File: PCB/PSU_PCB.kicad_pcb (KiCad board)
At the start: 2 copper layers, 169.3 x 128 mm, 130 parts, among them CON1 BARREL_JACK, IC1 ATMEGA328-P, P1 USB_OTG, P2 FTDI, P3 V+, P4 V-, P5 ISP, P6 I2C, P7 LCD_Display, Q1 TIP32CG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

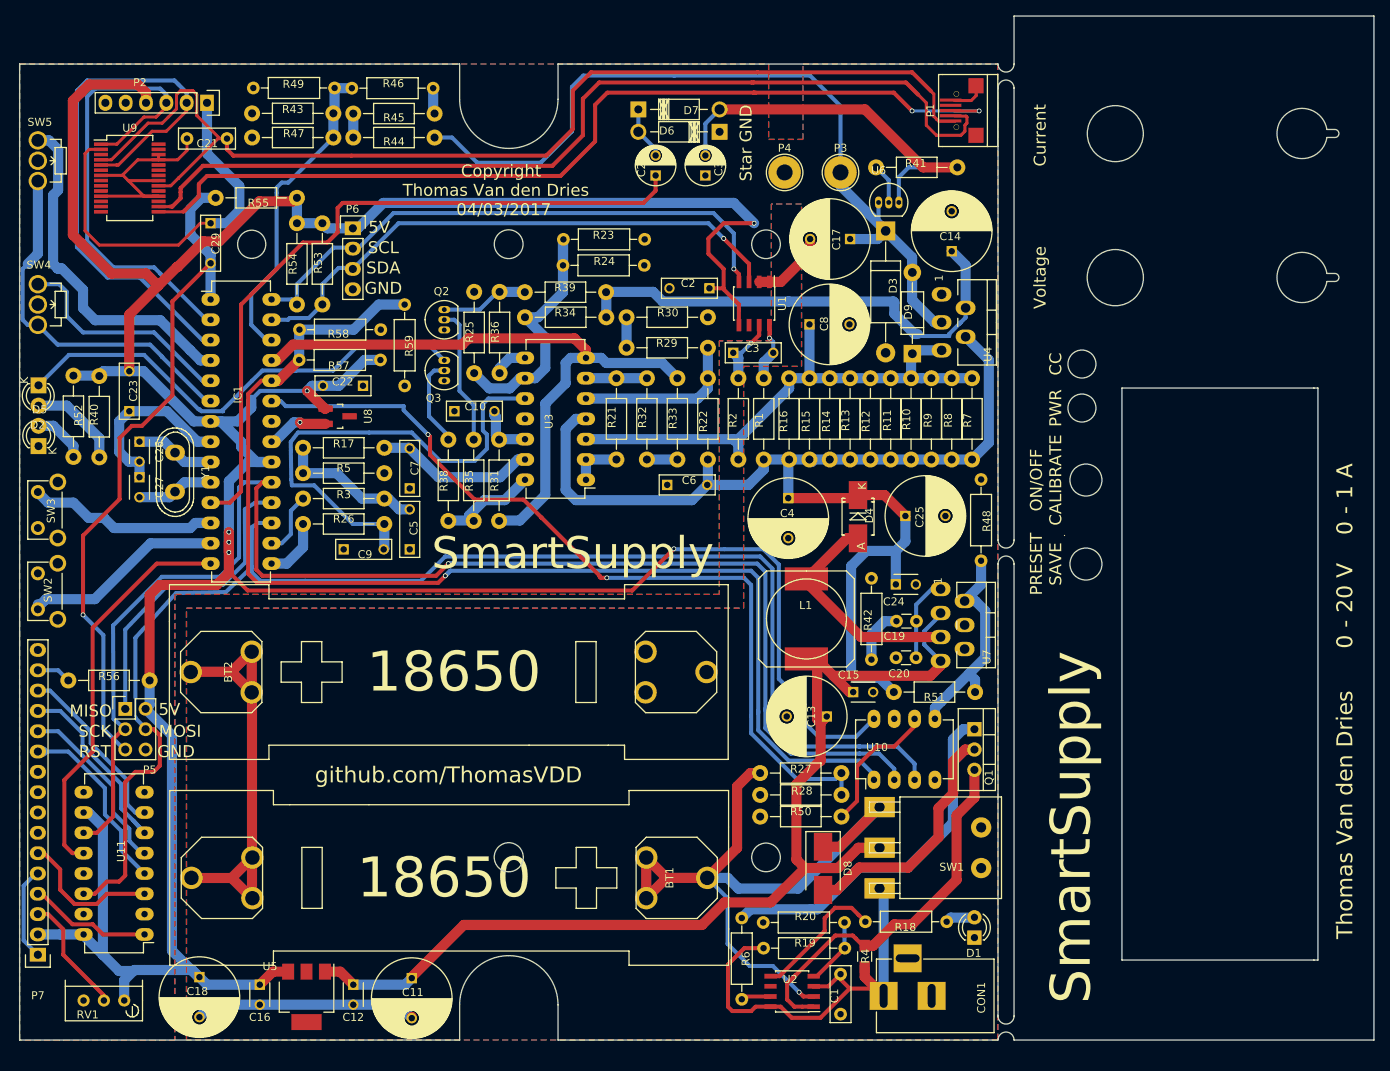
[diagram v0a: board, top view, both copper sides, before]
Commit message: Added protection resistor to charging circuitry
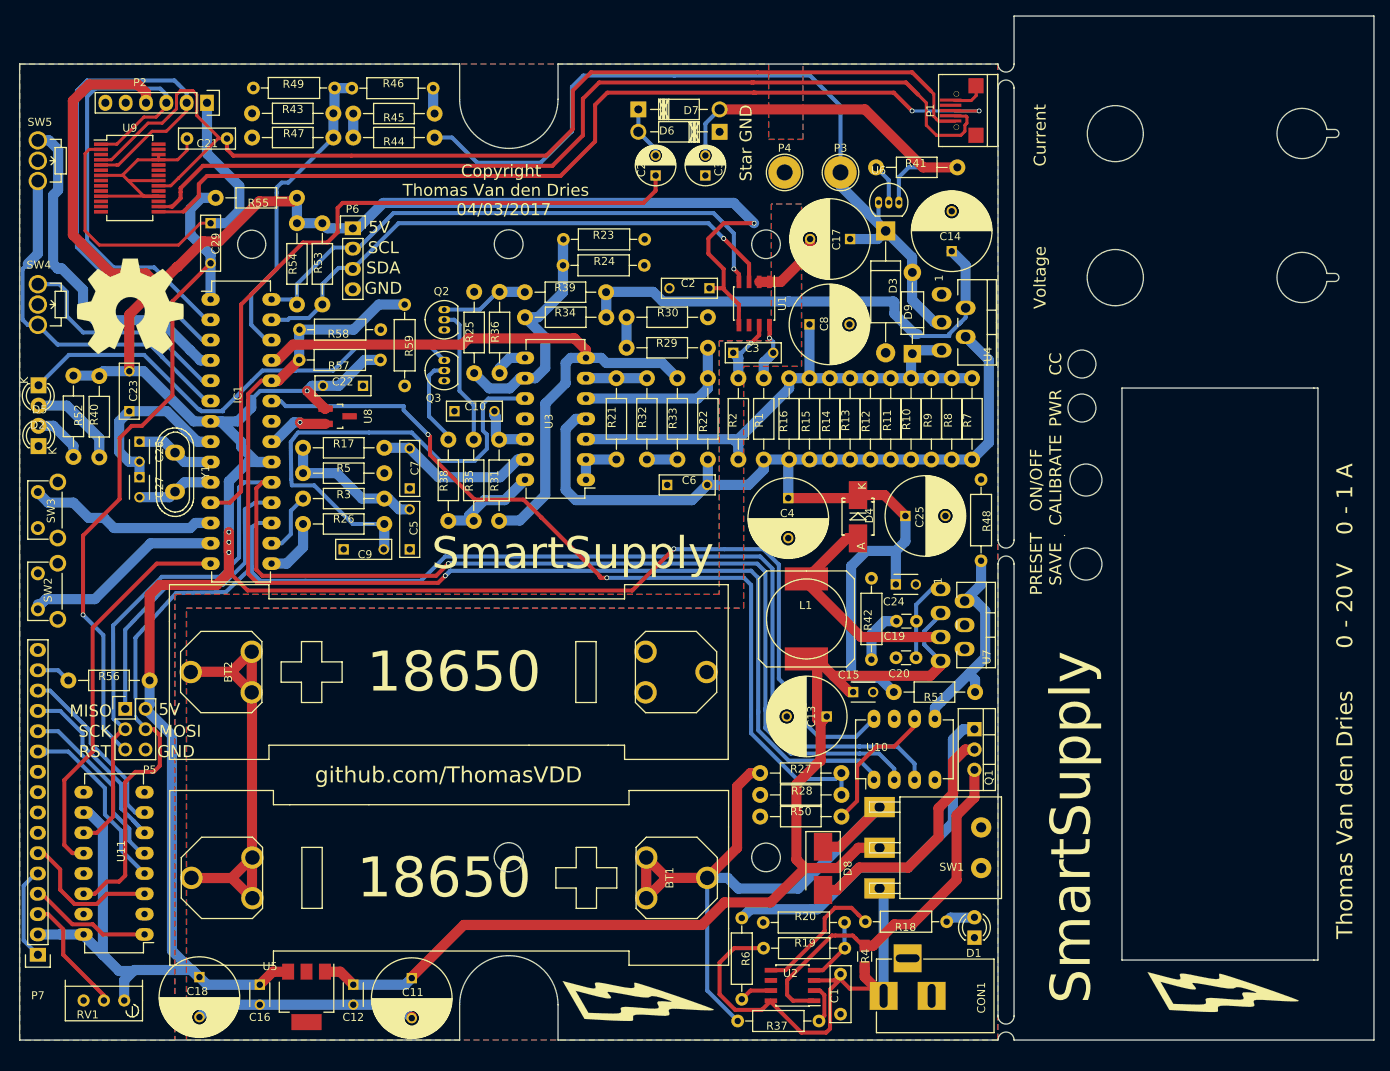
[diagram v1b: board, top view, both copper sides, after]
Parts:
- added G***: LOGO, Lightning:Lightning, F.Cu at (125.1, 149.7)
- added G***: LOGO, Lightning:Lightning, F.Cu at (198.2, 148.6)
- added R37: 10k, Resistors_ThroughHole:R_Axial_DIN0207_L6.3mm_D2.5mm_P10.16mm_Horizontal, F.Cu at (147.6, 152.6)
- added REF***: OSHW-Symbol_13.4x12mm_SilkScreen, Symbols:OSHW-Symbol_13.4x12mm_SilkScreen, F.Cu at (61.5, 63.3)
- moved U2 0.75 mm to (144.3, 148.2)
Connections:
- U2 pad 2: Net-(BT1-Pad1) -> Net-(R37-Pad1)
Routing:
- net +12V: track 57.8 -> 63.7 mm
- net Net-(R37-Pad1): track 0.00 -> 5.04 mm
- net Net-(BT1-Pad1): track 92.1 -> 88.8 mm, vias 1 -> 0

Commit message: Small BOM optimisation
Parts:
- C17, C8: value 2u2 -> 22u
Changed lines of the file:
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@@
       (effects (font (size 1 1) (thickness 0.15)))
     )
-    (fp_text value 2u2 (at 3.105 -0.058 270) (layer F.Fab)
+    (fp_text value 22u (at 3.105 -0.058 270) (layer F.Fab)
       (effects (font (size 1 1) (thickness 0.15)))
     )
@@
       (effects (font (size 1 1) (thickness 0.15)))
     )
-    (fp_text value 2u2 (at 3.245 0.058 90) (layer F.Fab)
-      (effects (font (size 1 1) (thickness 0.15)))
-    )
+    (fp_text value 22u (at 3.245 0.058 90) (layer F.Fab)
+      (effects (font (size 1 1) (thickness 0.15)))
+    )

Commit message: Esthetic change
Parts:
- moved SW5 1.00 mm to (50.0, 41.5)
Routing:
- net Net-(IC1-Pad4): track 43.7 -> 44.7 mm
- net Net-(IC1-Pad6): track 45.9 -> 46.9 mm
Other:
- outline, holes or cut-outs redrawn
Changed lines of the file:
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@@
     (links 303)
     (no_connects 0)
-    (area 47.694999 26.994999 216.995001 155.005001)
+    (area 47.534999 26.994999 216.995001 155.286001)
     (thickness 1.6)
     (drawings 81)
-    (tracks 1081)
+    (tracks 1082)
     (zones 0)
     (modules 134)
@@
   )
   (setup
-    (last_trace_width 0.25)
+    (last_trace_width 1.27)
     (user_trace_width 0.001)
     (user_trace_width 0.254)
@@
   )
   (module Potentiometers:Potentiometer_WirePads_Small (layer F.Cu)
-    (at 49.9745 42.545)
+    (at 49.96 41.55)
     (descr "Potentiometer, Wire Pads only, small, RevA, 02 Aug 2010,")
     (tags "Potentiometer, Wire Pads only, small, RevA, 02 Aug 2010,")
@@
     (effects (font (size 2 2) (thickness 0.3)))
   )
-  (gr_line (start 212.11 41.18) (end 211.11 41.18) (angle 90) (layer Edge.Cuts) (width 0.01))
-  (gr_line (start 212.11 42.18) (end 211.11 42.18) (angle 90) (layer Edge.Cuts) (width 0.01))
-  (gr_arc (start 212.11 41.68) (end 212.11 41.18) (angle 180) (layer Edge.Cuts) (width 0.01))
-  (gr_arc (start 208.01 41.68) (end 211.11 42.18) (angle 341.6) (layer Edge.Cuts) (width 0.01))
+  (gr_line (start 212.11 40.19) (end 211.11 40.19) (angle 90) (layer Edge.Cuts) (width 0.01))
+  (gr_line (start 212.11 41.19) (end 211.11 41.19) (angle 90) (layer Edge.Cuts) (width 0.01))
+  (gr_arc (start 212.11 40.69) (end 212.11 40.19) (angle 180) (layer Edge.Cuts) (width 0.01))
+  (gr_arc (start 208.01 40.69) (end 211.11 41.19) (angle 341.6) (layer Edge.Cuts) (width 0.01))
   (gr_arc (start 208.01 59.68) (end 211.11 60.18) (angle 341.6) (layer Edge.Cuts) (width 0.01))
   (gr_arc (start 212.11 59.68) (end 212.11 59.18) (angle 180) (layer Edge.Cuts) (width 0.01))
@@
   (gr_line (start 212.11 59.18) (end 211.11 59.18) (angle 90) (layer Edge.Cuts) (width 0.01))
   (gr_circle (center 184.66 59.7) (end 184.96 63.2) (layer Edge.Cuts) (width 0.15))
-  (gr_circle (center 184.66 41.7) (end 184.66 45.2) (layer Edge.Cuts) (width 0.15))
+  (gr_circle (center 184.66 40.71) (end 184.66 44.21) (layer Edge.Cuts) (width 0.15))
   (gr_circle (center 180.49 70.5) (end 180.49 72.25) (layer Edge.Cuts) (width 0.15))
   (gr_circle (center 180.49 76) (end 180.49 77.75) (layer Edge.Cuts) (width 0.15))
@@
     (effects (font (size 5 5) (thickness 0.3)))
   )
-  (gr_text Current (at 175.26 41.91 90) (layer F.SilkS)
+  (gr_text Current (at 175.26 40.92 90) (layer F.SilkS)
     (effects (font (size 1.5 1.5) (thickness 0.3)))
   )
@@
   (segment (start 53.594 61.468) (end 52.646 60.52) (width 0.508) (layer B.Cu) (net 19))
   (segment (start 52.646 60.52) (end 49.98 60.52) (width 0.508) (layer B.Cu) (net 19))
-  (segment (start 49.98 47.6305) (end 49.98 56.71) (width 1.27) (layer B.Cu) (net 20))
-  (segment (start 48.075 64.965) (end 48.71 65.6) (width 0.508) (layer B.Cu) (net 20))
-  (segment (start 48.075 58.615) (end 48.075 64.965) (width 0.508) (layer B.Cu) (net 20))
-  (segment (start 48.71 57.98) (end 48.075 58.615) (width 0.508) (layer B.Cu) (net 20))
-  (segment (start 49.98 56.71) (end 48.71 57.98) (width 1.27) (layer B.Cu) (net 20))
+  (segment (start 49.96 46.63) (end 49.96 56.69) (width 1.27) (layer B.Cu) (net 20))
   (segment (start 48.71 65.6) (end 49.98 65.6) (width 0.508) (layer B.Cu) (net 20))
-  (segment (start 49.98 47.6305) (end 49.9745 47.625) (width 1.27) (layer B.Cu) (net 20))
+  (segment (start 49.98 56.71) (end 48.71 57.98) (width 1.27) (layer B.Cu) (net 20))
+  (segment (start 48.71 57.98) (end 48.075 58.615) (width 0.508) (layer B.Cu) (net 20))
+  (segment (start 48.075 58.615) (end 48.075 64.965) (width 0.508) (layer B.Cu) (net 20))
+  (segment (start 48.075 64.965) (end 48.71 65.6) (width 0.508) (layer B.Cu) (net 20))
+  (segment (start 49.96 56.69) (end 49.98 56.71) (width 1.27) (layer B.Cu) (net 20))
   (segment (start 65.514 69.614) (end 65.514 69.578) (width 0.508) (layer B.Cu) (net 20))
   (segment (start 65.514 69.578) (end 64.008 68.072) (width 0.508) (layer B.Cu) (net 20))
@@
   (segment (start 71.025 75.125) (end 65.514 69.614) (width 0.508) (layer B.Cu) (net 20))
   (segment (start 65.514 69.614) (end 65.46 69.56) (width 0.508) (layer B.Cu) (net 20))
-  (segment (start 51.885 57.98) (end 51.885 49.3975) (width 1.27) (layer B.Cu) (net 21))
-  (segment (start 52.4515 58.5465) (end 51.885 57.98) (width 1.27) (layer B.Cu) (net 21))
-  (segment (start 51.3715 42.545) (end 49.9745 42.545) (width 1.27) (layer B.Cu) (net 21))
-  (segment (start 52.5145 43.688) (end 51.3715 42.545) (width 1.27) (layer B.Cu) (net 21))
-  (segment (start 52.5145 48.768) (end 52.5145 43.688) (width 1.27) (layer B.Cu) (net 21))
+  (segment (start 52.5145 43.688) (end 52.5145 42.6745) (width 1.27) (layer B.Cu) (net 21))
   (segment (start 51.885 49.3975) (end 52.5145 48.768) (width 1.27) (layer B.Cu) (net 21))
+  (segment (start 52.5145 48.768) (end 52.5145 43.688) (width 1.27) (layer B.Cu) (net 21))
+  (segment (start 52.4515 58.5465) (end 51.885 57.98) (width 1.27) (layer B.Cu) (net 21))
+  (segment (start 51.885 57.98) (end 51.885 49.3975) (width 1.27) (layer B.Cu) (net 21))
+  (segment (start 51.39 41.55) (end 49.96 41.55) (width 1.27) (layer B.Cu) (net 21))
+  (segment (start 52.5145 42.6745) (end 51.39 41.55) (width 1.27) (layer B.Cu) (net 21))
   (segment (start 52.4515 58.5465) (end 52.9585 58.5465) (width 1.27) (layer B.Cu) (net 21))
   (segment (start 70.3 70.045) (end 69.03 68.775) (width 1.27) (layer B.Cu) (net 21))
